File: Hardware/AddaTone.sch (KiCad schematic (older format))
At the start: 75 parts, among them J1 SWD_Header, J2 PItch_In, J3 PD1_Amt_In, J4 PD2_Amt_In, J5 VCA_In, J6 DAC1_Out, J7 DAC2_Out, J8 Eurorack_16_pin_power, SW3 Octave_Switch, U1 STM32F405RGTx, U2 MCP6004, U3 TL072, U4 LM1117-3.3, Y1 Crystal

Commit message: Added additional ADC channel for controlling harmonic level from CV
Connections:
- net labels added: HARM1_CV
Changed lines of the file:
@@
 $Comp
 L Amplifier_Operational:MCP6004 U2
-U 2 1 5C61BC1D
+U 1 1 5C61BC1D
 P 6050 2150
 F 0 "U2" H 6050 1783 50  0000 C CNN
@@
 F 2 "SMD_Packages:SOIC-14_N" H 6000 2250 50  0001 C CNN
 F 3 "http://ww1.microchip.com/downloads/en/DeviceDoc/21733j.pdf" H 6100 2350 50  0001 C CNN
-	2    6050 2150
+	1    6050 2150
 	1    0    0    1
 $EndComp
@@
 $Comp
 L Amplifier_Operational:MCP6004 U2
-U 1 1 5C76CA95
+U 2 1 5C76CA95
 P 6050 3950
 F 0 "U2" H 6050 3583 50  0000 C CNN
@@
 F 2 "SMD_Packages:SOIC-14_N" H 6000 4050 50  0001 C CNN
 F 3 "http://ww1.microchip.com/downloads/en/DeviceDoc/21733j.pdf" H 6100 4150 50  0001 C CNN
-	1    6050 3950
+	2    6050 3950
 	1    0    0    1
 $EndComp
@@
 $EndComp
 Text GLabel 6700 3950 2    50   Input ~ 0
-PD1_CV
+HARM1_CV
 Wire Wire Line
 	6700 3950 6350 3950
@@
 	3250 6900 3250 7050
 Text GLabel 3400 2100 2    50   Input ~ 0
-PD1_TYPE
+HARM1_CV
 Wire Wire Line
 	3250 3800 3400 3800

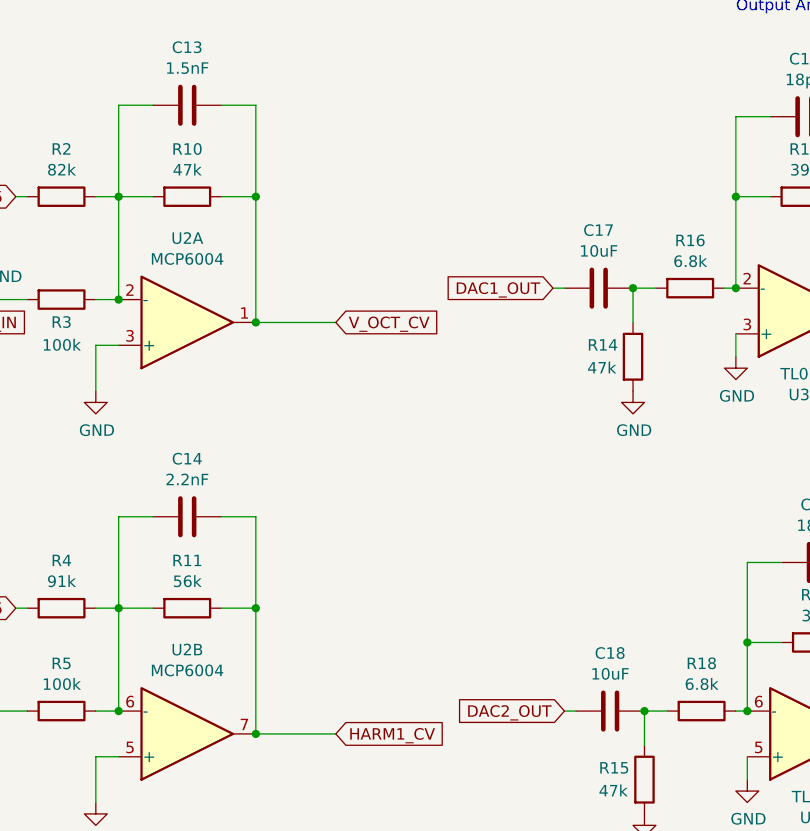
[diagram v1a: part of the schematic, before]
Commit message: Transferred ADC MCU to STM32L152; tweaks to comb filtering
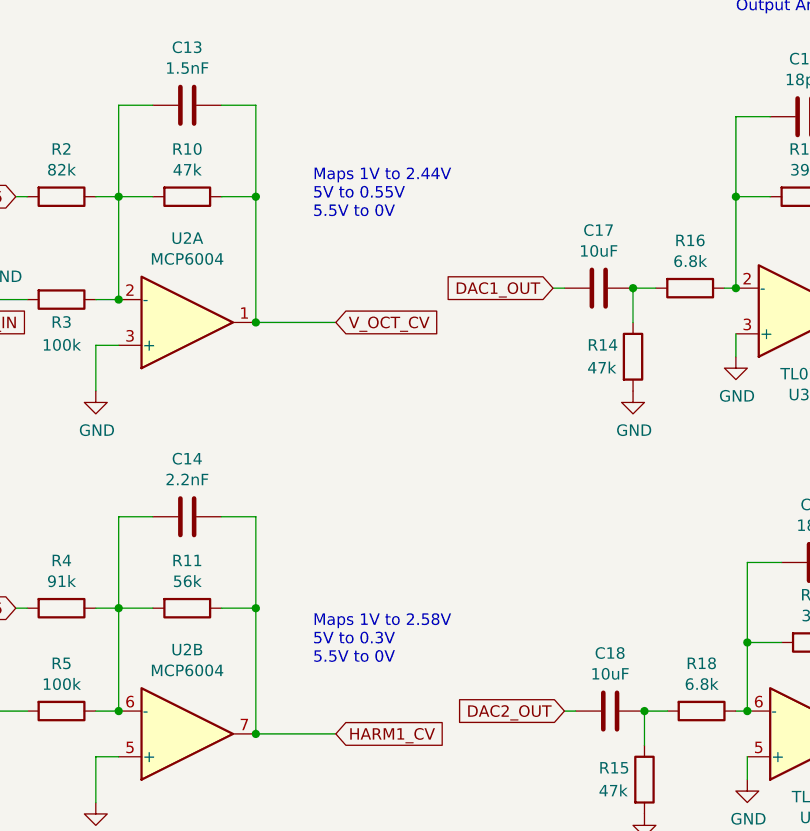
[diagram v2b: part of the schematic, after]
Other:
- note added: "Maps 1V to 2.44V\n5V to 0.55V\n5.5V to 0V"
- note added: "Maps 1V to 2.58V\n5V to 0.3V\n5.5V to 0V"
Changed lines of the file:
@@
 	1    0    0    -1
 $EndComp
+Text Notes 6600 3650 0    50   ~ 0
+Maps 1V to 2.58V\n5V to 0.3V\n5.5V to 0V
+Text Notes 6600 1700 0    50   ~ 0
+Maps 1V to 2.44V\n5V to 0.55V\n5.5V to 0V
 $EndSCHEMATC

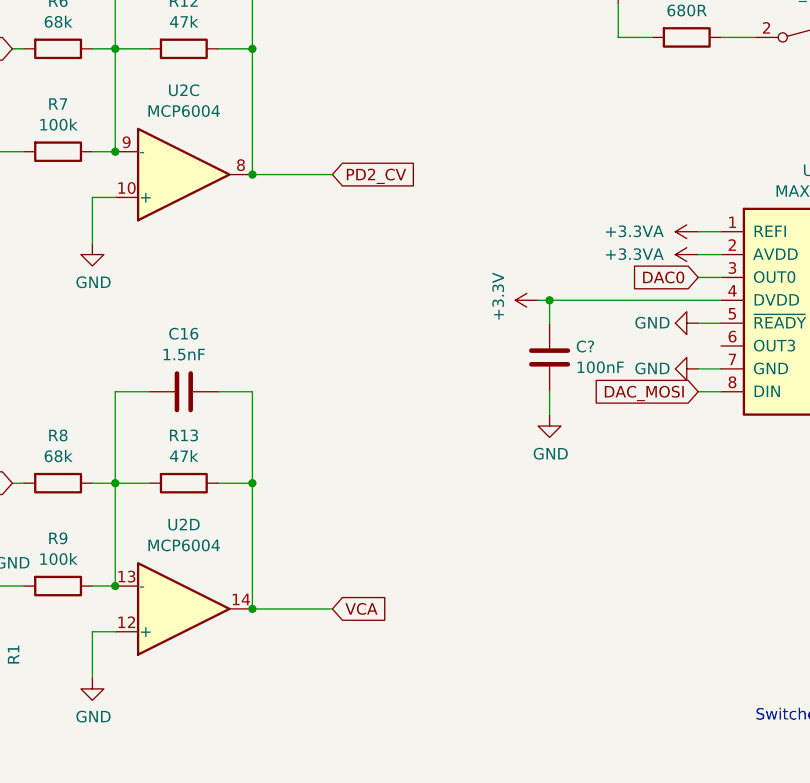
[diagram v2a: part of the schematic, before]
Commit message: Improved resolution of harmonic scale; Fixed issues with frequency scaling
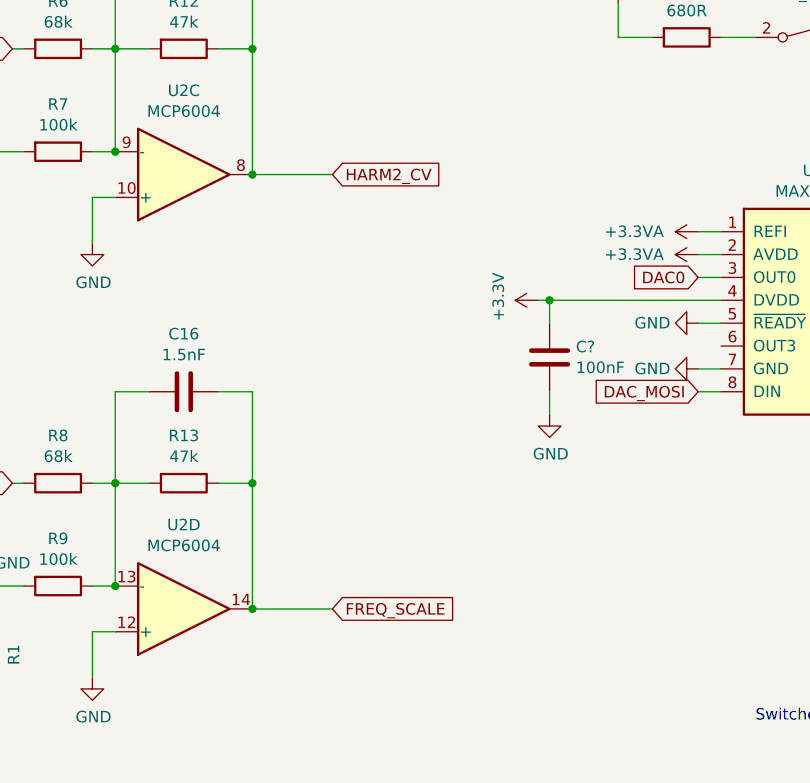
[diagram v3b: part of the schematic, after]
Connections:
- net labels added: FREQ_SCALE, HARM2_CV
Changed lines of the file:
@@
 	0    -1   -1   0
 $EndComp
-Text GLabel 6700 5850 2    50   Input ~ 0
-PD2_CV
+Text GLabel 6700 7750 2    50   Input ~ 0
+FREQ_SCALE
 Wire Wire Line
 	6700 5850 6350 5850
@@
 	0    -1   -1   0
 $EndComp
-Text GLabel 6700 7750 2    50   Input ~ 0
-VCA
+Text GLabel 6700 5850 2    50   Input ~ 0
+HARM2_CV
 Wire Wire Line
 	6700 7750 6350 7750

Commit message: Rev 2 of dev board; provisional handling for overflow on output samples
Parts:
- removed C8: 2.2uF, Capacitors_SMD:C_0805_HandSoldering, symbol Device:C
- removed L1: L, Resistors_SMD:R_0805_HandSoldering, symbol Device:L
- removed R1: 47k, Resistors_SMD:R_0805_HandSoldering, symbol Device:R
- removed U1: STM32F405RGTx, Package_QFP:LQFP-64_10x10mm_P0.5mm, symbol MCU_ST_STM32F4:STM32F405RGTx
- removed U4: LM1117-3.3, TO_SOT_Packages_SMD:TO-252-3_TabPin2, symbol Regulator_Linear:LM1117-3.3
- removed U?: MachX03D-9400C, symbol Lattice_MachX03D:MachX03D-9400C
- added C?: 10uF, Capacitors_SMD:CP_Elec_5x5.8, symbol Device:C
- added C? (x5): 1uF, Capacitors_SMD:C_0805_HandSoldering, symbol Device:C
- added C? (x4): 10nF, Capacitors_SMD:C_0805_HandSoldering, symbol Device:C
- added C? (x6): 100nF, Capacitors_SMD:C_0805_HandSoldering, symbol Device:C
- added C?: 10uF, Capacitors_SMD:C_0805_HandSoldering, symbol Device:C
- added D?: MBR130T1G, symbol Device:D_Schottky
- added L?: L, Resistors_SMD:R_0805_HandSoldering, symbol Device:L
- added R?: 100, Resistors_SMD:R_0805_HandSoldering, symbol Device:R
- added U?: STM32F446RETx, Package_QFP:LQFP-64_10x10mm_P0.5mm, symbol MCU_ST_STM32F4:STM32F446RETx
- added U?: MIC5355-S4YMME, Package_SO:MSOP-8-1EP_3x3mm_P0.65mm_EP2.5x3mm_Mask1.73x2.36mm_ThermalVias, symbol Regulator_Linear:MIC5355-S4YMME
- added U?: ICE40UP5K-SG48ITR, Package_DFN_QFN:QFN-48-1EP_7x7mm_P0.5mm_EP5.6x5.6mm, symbol ICE40UP5K:ICE40UP5K-SG48ITR-Merged
- added U?: LM1117-5.0, symbol Regulator_Linear:LM1117-5.0
- C?: renamed from C25; value 47uF -> 22uF
- C?: renamed from C21; value 47uF -> 10uF
- Y?: renamed from Y1; value Crystal -> ECS-12MHz
- renumbered C5 to C?, C2 to C?, C3 to C?, C1 to C?, C4 to C?, C9 to C?, C10 to C?, C13 to C?, C24 to C?, C14 to C?, C18 to C?, C15 to C?, C16 to C?, C22 to C?, C17 to C?, C23 to C?, C20 to C?, C19 to C?, C6 to C?, C7 to C?, C11 to C?, C12 to C?, CTune1 to CTune?, D1 to D?, D2 to D?, D3 to D?, FTune1 to FTune?, J1 to J?, J2 to J?, J8 to J?, J3 to J?, J4 to J?, J5 to J?, J6 to J?, J7 to J?, PD1Amt1 to PD1Amt?, PD1Type1 to PD1Type?, PD2Amt1 to PD2Amt?, PD2Type1 to PD2Type?, R10 to R?, R2 to R?, R3 to R?, R25 to R?, R11 to R?, R4 to R?, R5 to R?, R24 to R?, R20 to R?, R15 to R?, R18 to R?, R12 to R?, R6 to R?, R7 to R?, R13 to R?, R8 to R?, R9 to R?, R17 to R?, R23 to R?, R19 to R?, R14 to R?, R16 to R?, SW3 to SW?, U2 to U?, U3 to U?
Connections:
- net labels added: +1V2, +5V, ADC_CS, ADC_Clock, ADC_Data, DAC_CLK, FPGA_DONE, FPGA_RESET, FPGA_SCK, FPGA_SI, FPGA_SS, FREQ_SC_POT, HARM1_POT, HARM2_POT, HARM_COUNT, MCO2_CLOCK_OUT, RESET, VCCIO_0, VCCIO_1, VCCIO_2
- net labels removed: DAC+CLK, DAC2_MIX, PD1_CV, PD1_POT, PD1_TYPE, PD2_CV, PD2_POT, PD2_TYPE, VCA
- wire segments 270 -> 357
- no-connect marks 40 -> 30
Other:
- moved on the sheet: C?, CTune?, D?, FTune?, J?, PD1Amt?, PD1Type?, PD2Amt?, PD2Type?, R?, SW?, U?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

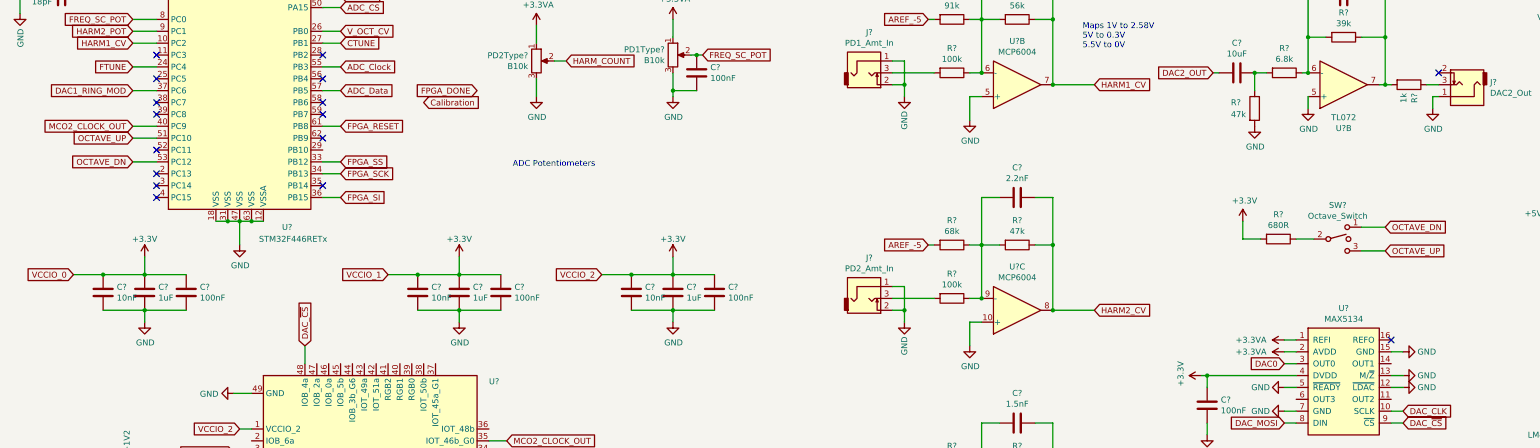
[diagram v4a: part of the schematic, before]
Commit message: Implemented Mix switch
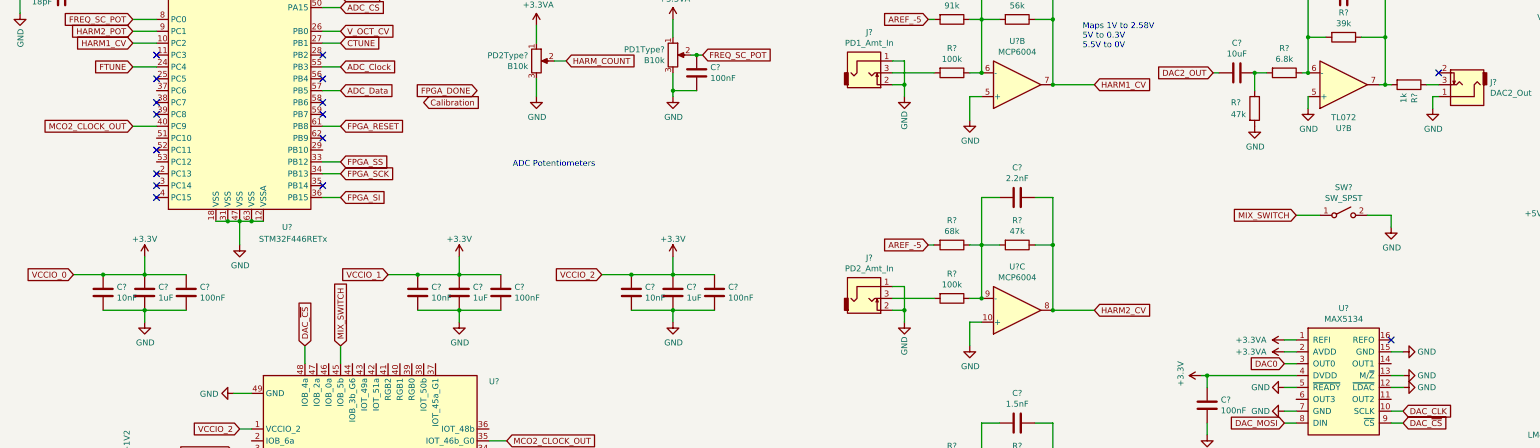
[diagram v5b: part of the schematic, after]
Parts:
- removed R?: 680R, Resistors_SMD:R_0805_HandSoldering, symbol Device:R
- removed SW?: Octave_Switch, Custom_Footprints:SPDTSubMiniature, symbol Switch:SW_SPDT_MSM
- added SW?: SW_SPST, symbol Switch:SW_SPST
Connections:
- net GND: now also SW?.2 (B)
- net MIX_SWITCH: now reaches U?.45 (IOB_5b)
- net MIX_SWITCH: now also SW?.1 (A)
- net DAC1_RING_MOD: no longer names the net of U?.37 (PC6)
- net OCTAVE_DN: no longer names the net of U?.53 (PC12)
- net OCTAVE_UP: no longer names the net of U?.51 (PC10)
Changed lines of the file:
@@
 Text GLabel 1650 3800 0    50   Input ~ 0
 HARM1_CV
-Text GLabel 1650 4200 0    50   Input ~ 0
-DAC1_RING_MOD
-Wire Wire Line
-	1650 4200 1850 4200
+Text GLabel 11450 5250 0    50   Input ~ 0
+MIX_SWITCH
 $Comp
 L Device:R_POT PD1Type?
@@
 Wire Wire Line
 	1650 3600 1850 3600
-$Comp
-L Switch:SW_SPDT_MSM SW?
-U 1 1 5C8C13F5
-P 11800 5450
-F 0 "SW?" H 11800 5735 50  0000 C CNN
-F 1 "Octave_Switch" H 11800 5644 50  0000 C CNN
-F 2 "Custom_Footprints:SPDTSubMiniature" H 11800 5450 50  0001 C CNN
-F 3 "" H 11800 5450 50  0001 C CNN
-	1    11800 5450
-	1    0    0    -1
-$EndComp
-$Comp
-L Device:R R?
-U 1 1 5C8C15C8
-P 11300 5450
-F 0 "R?" V 11093 5450 50  0000 C CNN
-F 1 "680R" V 11184 5450 50  0000 C CNN
-F 2 "Resistors_SMD:R_0805_HandSoldering" V 11230 5450 50  0001 C CNN
-F 3 "~" H 11300 5450 50  0001 C CNN
-	1    11300 5450
-	0    1    1    0
-$EndComp
-Wire Wire Line
-	11450 5450 11600 5450
-$Comp
-L power:+3.3V #PWR0121
-U 1 1 5C8C94A6
-P 11000 5300
-F 0 "#PWR0121" H 11000 5150 50  0001 C CNN
-F 1 "+3.3V" H 11015 5473 50  0000 C CNN
-F 2 "" H 11000 5300 50  0001 C CNN
-F 3 "" H 11000 5300 50  0001 C CNN
-	1    11000 5300
-	1    0    0    -1
-$EndComp
-Wire Wire Line
-	11000 5300 11000 5450
-Wire Wire Line
-	11000 5450 11150 5450
-Text GLabel 12200 5550 2    50   Input ~ 0
-OCTAVE_UP
-Text GLabel 12200 5350 2    50   Input ~ 0
-OCTAVE_DN
-Wire Wire Line
-	12000 5350 12200 5350
-Wire Wire Line
-	12000 5550 12200 5550
-Text GLabel 1650 4600 0    50   Input ~ 0
-OCTAVE_UP
-Text GLabel 1650 4800 0    50   Input ~ 0
-OCTAVE_DN
 $Comp
 L Amplifier_Operational:TL072 U?
@@
 Wire Wire Line
 	16100 1000 16100 1050
-Wire Wire Line
-	1650 4800 1850 4800
-Wire Wire Line
-	1650 4600 1850 4600
 NoConn ~ 3250 5000
 Text GLabel 4100 4300 2    50   Input ~ 0
@@
 Wire Wire Line
 	8150 7950 8150 8100
+$Comp
+L Switch:SW_SPST SW?
+U 1 1 5E8B1CBD
+P 11850 5250
+F 0 "SW?" H 11850 5485 50  0000 C CNN
+F 1 "SW_SPST" H 11850 5394 50  0000 C CNN
+F 2 "" H 11850 5250 50  0001 C CNN
+F 3 "~" H 11850 5250 50  0001 C CNN
+	1    11850 5250
+	1    0    0    -1
+$EndComp
+$Comp
+L power:GND #PWR?
+U 1 1 5E8B261E
+P 12250 5350
+F 0 "#PWR?" H 12250 5100 50  0001 C CNN
+F 1 "GND" H 12255 5177 50  0000 C CNN
+F 2 "" H 12250 5350 50  0001 C CNN
+F 3 "" H 12250 5350 50  0001 C CNN
+	1    12250 5350
+	1    0    0    -1
+$EndComp
+Wire Wire Line
+	11450 5250 11650 5250
+Wire Wire Line
+	12050 5250 12250 5250
+Wire Wire Line
+	12250 5250 12250 5350
+Text GLabel 3400 6350 1    50   Input ~ 0
+MIX_SWITCH
+Wire Wire Line
+	3400 6350 3400 6500
 $EndSCHEMATC

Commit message: Updates to schematic
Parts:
- removed C? (x4): 100nF, Capacitors_SMD:C_0805_HandSoldering, symbol Device:C
- removed C? (x4): 1uF, Capacitors_SMD:C_0805_HandSoldering, symbol Device:C
- removed U?: MIC5355-S4YMME, Package_SO:MSOP-8-1EP_3x3mm_P0.65mm_EP2.5x3mm_Mask1.73x2.36mm_ThermalVias, symbol Regulator_Linear:MIC5355-S4YMME
- removed U?: LM1117-5.0, symbol Regulator_Linear:LM1117-5.0
- added C36: 10uF, Capacitors_SMD:CP_Elec_3x5.3, symbol Device:C
- added C?: 100nF, Capacitors_SMD:C_0805_HandSoldering, symbol Device:C
- added SW2: SW_SPST, Custom_Footprints:SPDTSubMiniature, symbol Switch:SW_SPST
- added SW3: SW_SPST, Custom_Footprints:SW_SPST_EVQQ2, symbol Switch:SW_SPST
- added SW4: SW_SPST, Buttons_Switches_THT:SW_PUSH_6mm, symbol Switch:SW_SPST
- added U6: LD1117S12TR_SOT223, TO_SOT_Packages_SMD:SOT-223, symbol Regulator_Linear:LD1117S12TR_SOT223
- added U7: LM1117-3.3, TO_SOT_Packages_SMD:SOT-223, symbol Regulator_Linear:LM1117-3.3
- C37, C42: renamed from C?; footprint Capacitors_SMD:CP_Elec_5x5.8 -> Capacitors_SMD:CP_Elec_3x5.3
- C39, C40: renamed from C?; footprint Capacitors_SMD:CP_Elec_4x5.8 -> Capacitors_SMD:CP_Elec_5x5.3
- C41: renamed from C?; value 22uF -> 47uF; footprint Capacitors_SMD:CP_Elec_5x5.8 -> Capacitors_SMD:CP_Elec_5x5.3
- D1: renamed from D?; footprint (none) -> Diodes_SMD:D_SOD-123
- L1: renamed from L?; footprint Resistors_SMD:R_0805_HandSoldering -> Inductors_SMD:L_0805_HandSoldering
- SW1: renamed from SW?; footprint (none) -> Custom_Footprints:SPDTSubMiniature
- Y1: renamed from Y?; footprint Custom_Footprints:Crystal_SMD -> Crystals:Crystal_SMD_0603-2pin_6.0x3.5mm_HandSoldering
- gave numbers to parts that had none: 73
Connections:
- net +5V is gone; now on net +3V3: C41.1
- net DAC0 is gone; now on net DAC1_OUT: U4.3 (OUT0)
- net +1V2: now also C42.1, C?.1, U6.2 (VO)
- net +3V3: now also U7.2 (VO); no longer C42.1
- net Calibration: now also U1.44 (PA11), SW3.1 (A)
- net DAC2_OUT: now also U4.14 (OUT1)
- net FPGA_DONE: now also U1.42 (PA9)
- net FREQ_SCALE: now also U1.22 (PA6)
- net FTUNE: now also U1.25 (PC5); no longer U1.24 (PC4)
- net GND: now also C?.2, SW2.2 (B), SW3.2 (B), SW4.2 (B), U6.1 (GND), U7.1 (GND); no longer C41.2
- net HARM1_CV: now also U1.11 (PC3); no longer U1.10 (PC2)
- net HARM2_POT: now also U1.10 (PC2); no longer U1.9 (PC1)
- net RESET: now also SW4.1 (A)
- net VCC: now also C36.1, U6.3 (VI), U7.3 (VI)
- net RING_MOD: now reaches U2.19 (IOB_29b)
- net RING_MOD: now also U1.24 (PC4), SW2.1 (A)
- new net: C36.2, C41.2
- no-connect marks 30 -> 59
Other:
- moved on the sheet: C11, C12, C14, C15, C16, C19, C20, C21, C25, C26, C31, C33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

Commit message: Updated schematic for PCM5100 DAC
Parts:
- removed U4: MAX5134, Housings_SSOP:TSSOP-16_4.4x5mm_Pitch0.65mm, symbol MAX5134:MAX5134
- removed unit 2 of U5
- added C13, C17, C24: 100nF, symbol Device:C
- added C18: 1nF, Capacitors_SMD:C_0805_HandSoldering, symbol Device:C
- added C22, C43: 10uF, symbol Device:C
- added C23: 100pF, Capacitors_SMD:C_0805_HandSoldering, symbol Device:C
- added U4: PCM5100APW, Package_SO:TSSOP-20_4.4x6.5mm_P0.65mm, symbol PCM5100APW:PCM5100APW
- added U8: TL072, SMD_Packages:SOIC-8-N, symbol Amplifier_Operational:TL072
- C31: value 100nF -> 2.2uF; footprint Capacitors_SMD:C_0805_HandSoldering -> (none)
- C32: value 10uF -> 1nF
- C33: value 10uF -> 2.2uF; footprint Capacitors_SMD:C_0805_HandSoldering -> (none)
- C34: value 18pF -> 100pF
- C35: value 18pF -> 100nF; footprint Capacitors_SMD:C_0805_HandSoldering -> (none)
- R14, R15: value 47k -> 2.2k
- R16, R17: value 6.8k -> 10k
- R18, R19: value 39k -> 33k
- gave numbers to parts that had none: 1
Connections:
- net +3.3VA: now also C13.1, C17.1, C22.1, U4.1 (CPVDD), U4.8 (AVDD)
- net +3V3: now also C24.1, C43.1, U4.11 (FLT), U4.17 (XSMT), U4.20 (DVDD); no longer C31.1
- net DAC1_OUT: now also R14.2, U4.6 (OUTL); no longer C32.2
- net DAC2_OUT: now also R15.2, U4.7 (OUTR); no longer C33.2
- net GND: now also C32.1, C33.2, C35.1, C13.2, C17.2, C18.1, C22.2, C24.2, C43.2, U4.10 (DEMP), U4.12 (SCK), U4.16 (FMT), U4.19 (DGND), U4.3 (CPGND), U4.9 (AGND), U8.3 (+); no longer C31.2, R14.2, R15.2
- net at R17.1, R19.2: now also C23.1, U8.2 (-); no longer C35.1
- net at R19.1, R21.2: now also C23.2, U8.1; no longer C35.2
- net at R15.1, R17.2: now also C18.2; no longer C33.1
- net at R14.1, R16.2: now also C32.2; no longer C32.1
- net DAC_CLK renamed DAC_BCLK
- net DAC_BCLK: now also U4.13 (BCK)
- net DAC_MOSI renamed DAC_DATA
- net DAC_DATA: now also U4.14 (DIN)
- net DAC_~CS renamed DAC_LRCLK
- net DAC_LRCLK: now also U4.15 (LRCK)
- new net: C31.1, U4.2 (CAPP)
- new net: C31.2, U4.4 (CAPM)
- new net: C33.1, U4.5 (VNEG)
- new net: C35.2, U4.18 (LDOO)
- no-connect marks 59 -> 56
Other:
- note removed: "Switches"
- moved on the sheet: C32, C36, C37, C38, C41, C42, D2, L1, R14, R22, SW1, SW2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
